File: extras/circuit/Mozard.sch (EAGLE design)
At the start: 42 parts, among them J4 Headphone/Line Out, U2 LM386

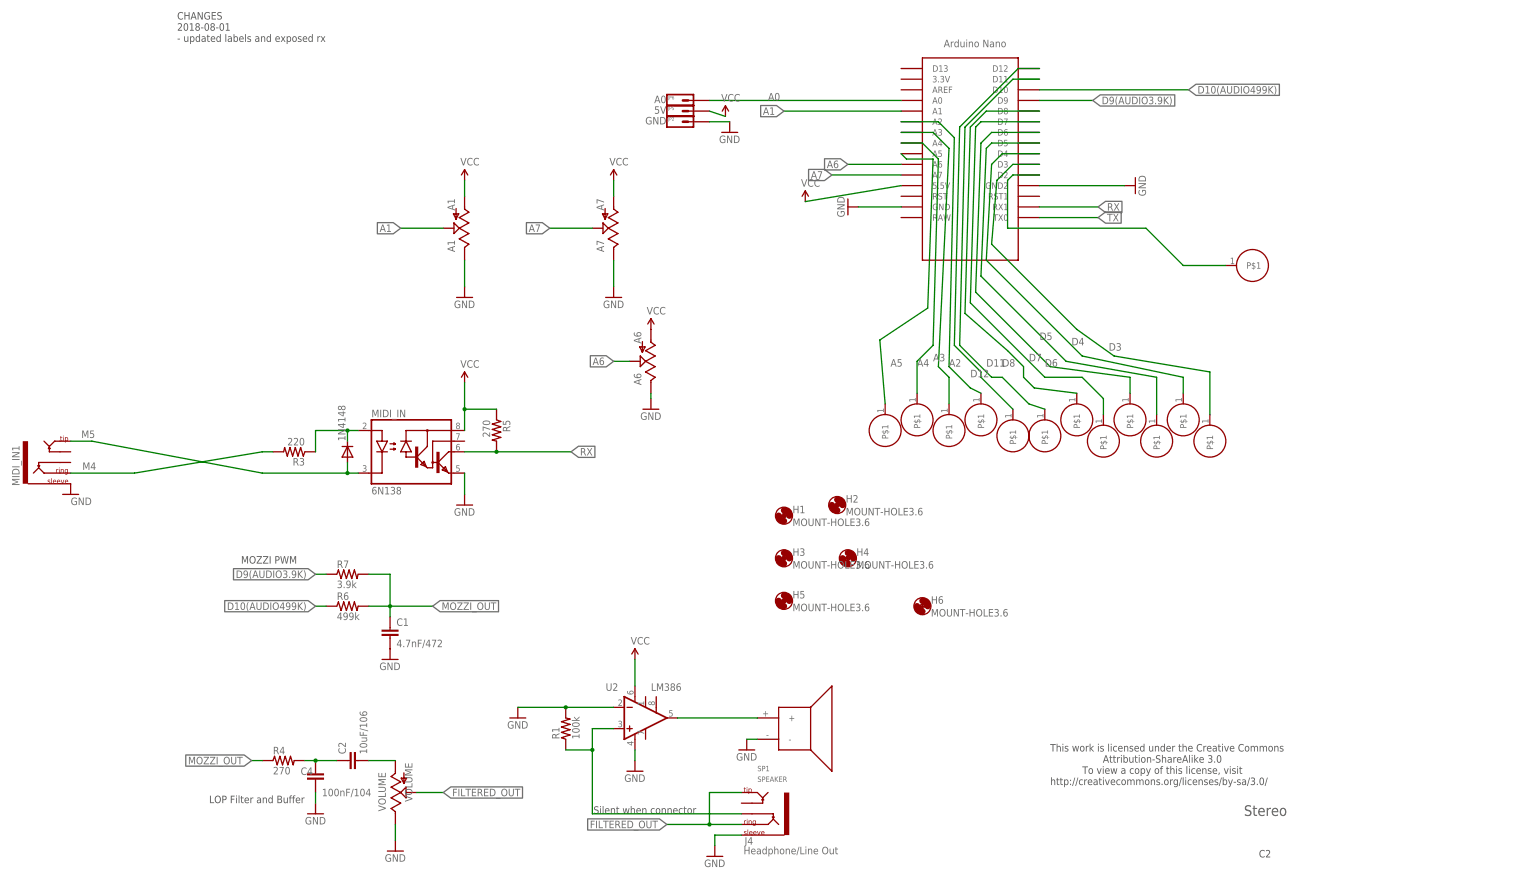
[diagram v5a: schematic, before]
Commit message: New board + poly
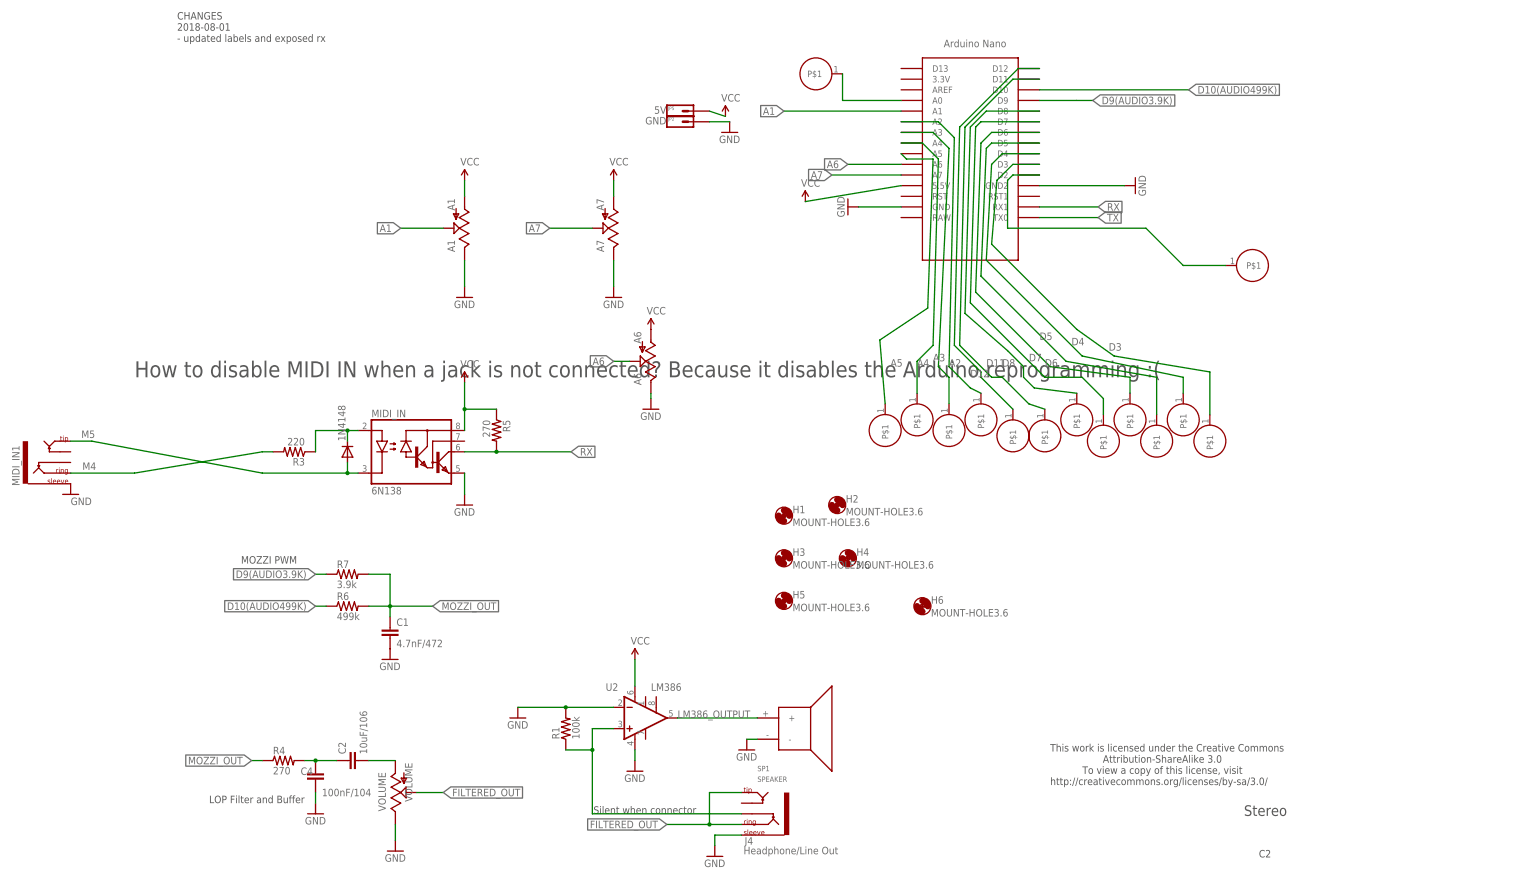
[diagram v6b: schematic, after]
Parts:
- removed JP6: A0, TOF:HEADER-1X1
- added U$15: PCB-TOUCHPAD-1-PIN, TOF:PCB-TOUCHPAD-1-PIN
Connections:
- net N$1 renamed LM386_OUTPUT
- removed net A0: JP6.1, U$1.A0
- new net N$3: U$1.A0, U$15.P$1
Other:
- note added: "How to disable MIDI IN when a jack is not connected? Because it disables the Arduino reprogramming :("
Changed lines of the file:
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@@
 <?xml version="1.0" encoding="utf-8"?>
 <!DOCTYPE eagle SYSTEM "eagle.dtd">
-<eagle version="9.3.1">
+<eagle version="9.5.0">
 <drawing>
 <settings>
@@
 <part name="JP2" library="TOF" deviceset="HEADER-1X1" device="" value="GND"/>
 <part name="JP5" library="TOF" deviceset="HEADER-1X1" device="" value="5V"/>
-<part name="JP6" library="TOF" deviceset="HEADER-1X1" device="" value="A0"/>
 <part name="A1" library="TOF" deviceset="POT" device="" value="A1"/>
 <part name="GND28" library="SparkFun-Aesthetics" deviceset="GND" device=""/>
@@
 <part name="SUPPLY3" library="SparkFun-Aesthetics" deviceset="VCC" device=""/>
 <part name="SUPPLY7" library="SparkFun-Aesthetics" deviceset="VCC" device=""/>
+<part name="U$15" library="TOF" deviceset="PCB-TOUCHPAD-1-PIN" device=""/>
 </parts>
 <sheets>
@@
 2018-08-01
 - updated labels and exposed rx</text>
+<text x="-2.54" y="121.92" size="3.81" layer="97">How to disable MIDI IN when a jack is not connected? Because it disables the Arduino reprogramming :(</text>
 </plain>
 <instances>
@@
 <attribute name="VALUE" x="124.333" y="186.563" size="1.778" layer="96" rot="R180"/>
 <attribute name="NAME" x="124.714" y="185.674" size="0.8128" layer="95"/>
-</instance>
-<instance part="JP6" gate="G$1" x="127" y="187.96" smashed="yes">
-<attribute name="VALUE" x="124.333" y="189.103" size="1.778" layer="96" rot="R180"/>
-<attribute name="NAME" x="124.714" y="188.214" size="0.8128" layer="95"/>
 </instance>
 <instance part="A1" gate="G$1" x="76.2" y="157.48" smashed="yes" rot="R180">
@@
 <attribute name="VALUE" x="75.184" y="124.206" size="1.778" layer="96"/>
 </instance>
+<instance part="U$15" gate="G$1" x="160.02" y="194.31" smashed="yes" rot="R180"/>
 </instances>
 <busses>
@@
 <wire x1="100.33" y1="33.02" x2="106.68" y2="33.02" width="0.1524" layer="91"/>
 <junction x="106.68" y="33.02"/>
-</segment>
-</net>
-<net name="A0" class="0">
-<segment>
-<pinref part="U$1" gate="G$1" pin="A0"/>
-<wire x1="180.34" y1="187.96" x2="134.62" y2="187.96" width="0.1524" layer="91"/>
-<label x="148.59" y="187.96" size="1.778" layer="95"/>
-<pinref part="JP6" gate="G$1" pin="1"/>
 </segment>
 </net>
@@
 </segment>
 </net>
-<net name="N$1" class="0">
+<net name="LM386_OUTPUT" class="0">
 <segment>
 <pinref part="U2" gate="G$1" pin="OUT"/>
 <pinref part="SP1" gate="G$1" pin="+"/>
 <wire x1="127" y1="40.64" x2="146.05" y2="40.64" width="0.1524" layer="91"/>
-</segment>
-</net>
+<label x="127" y="40.64" size="1.778" layer="95"/>
+</segment>
+</net>
+<net name="N$3" class="0">
+<segment>
+<pinref part="U$15" gate="G$1" pin="P$1"/>
+<pinref part="U$1" gate="G$1" pin="A0"/>
+<wire x1="166.37" y1="194.31" x2="166.37" y2="187.96" width="0.1524" layer="91"/>
+<wire x1="166.37" y1="187.96" x2="180.34" y2="187.96" width="0.1524" layer="91"/>
+</segment>
+</net>
